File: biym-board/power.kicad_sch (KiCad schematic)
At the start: 6 parts, among them J1 JST_SH_BM02_VERTICAL, Q1 MOSFET-N-CH-EN, Q2 MOSFET-P-CH-EN

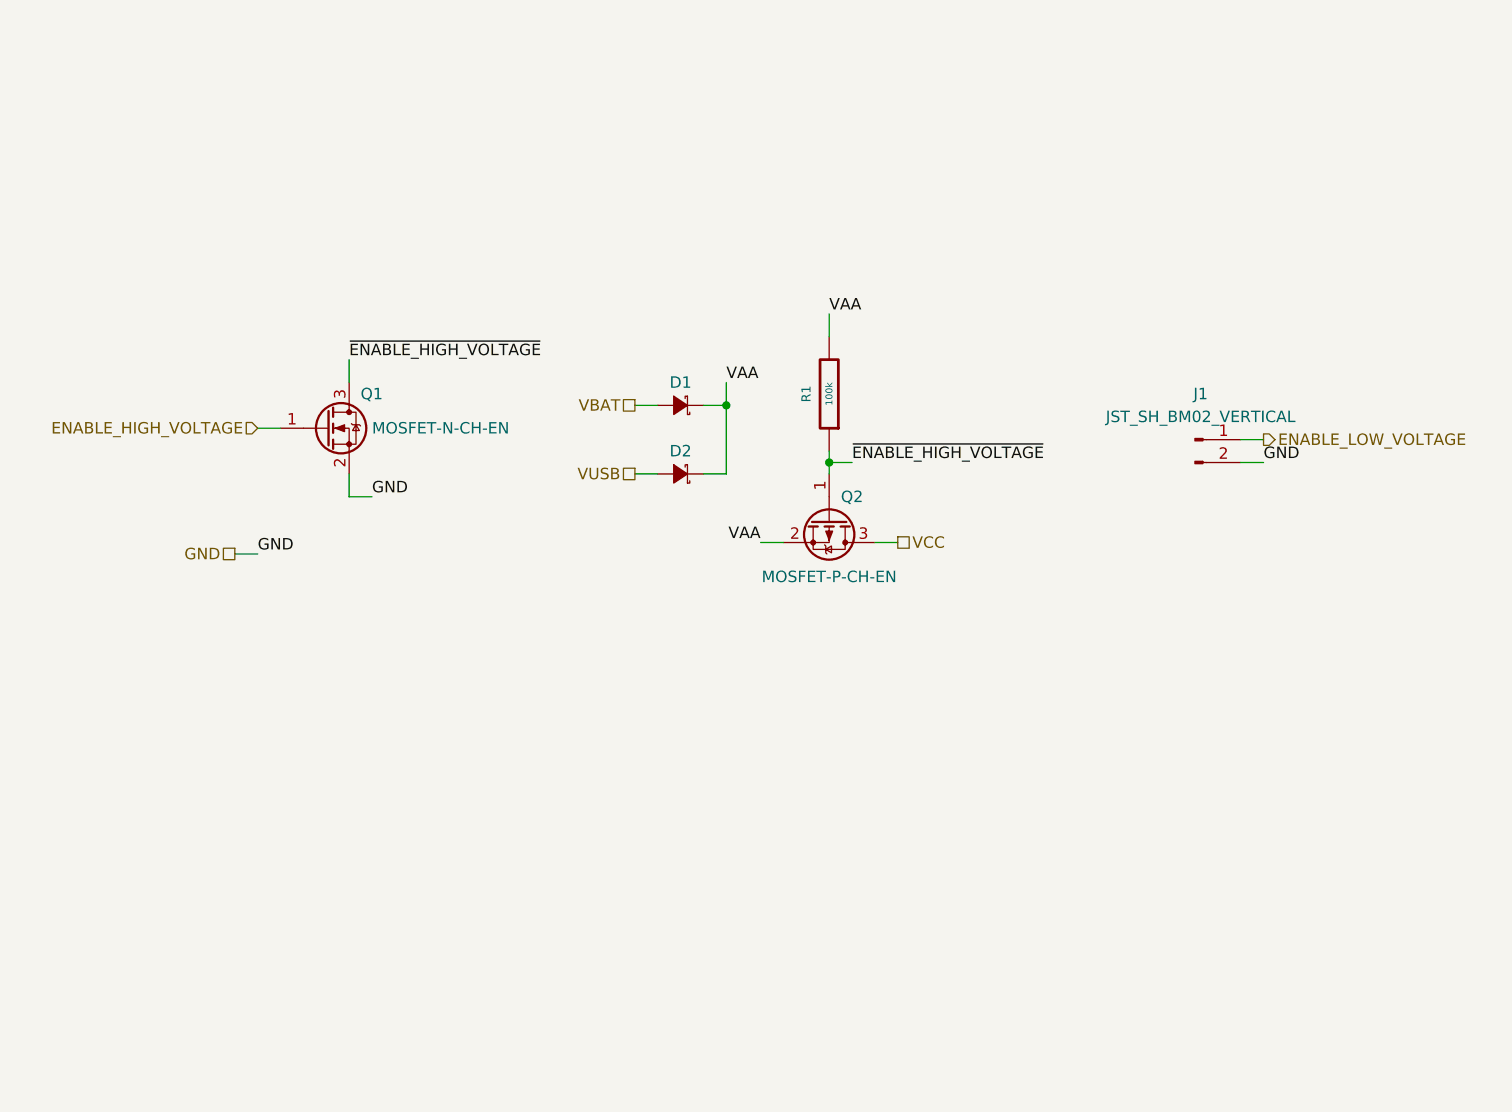
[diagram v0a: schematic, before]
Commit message: Change diodes
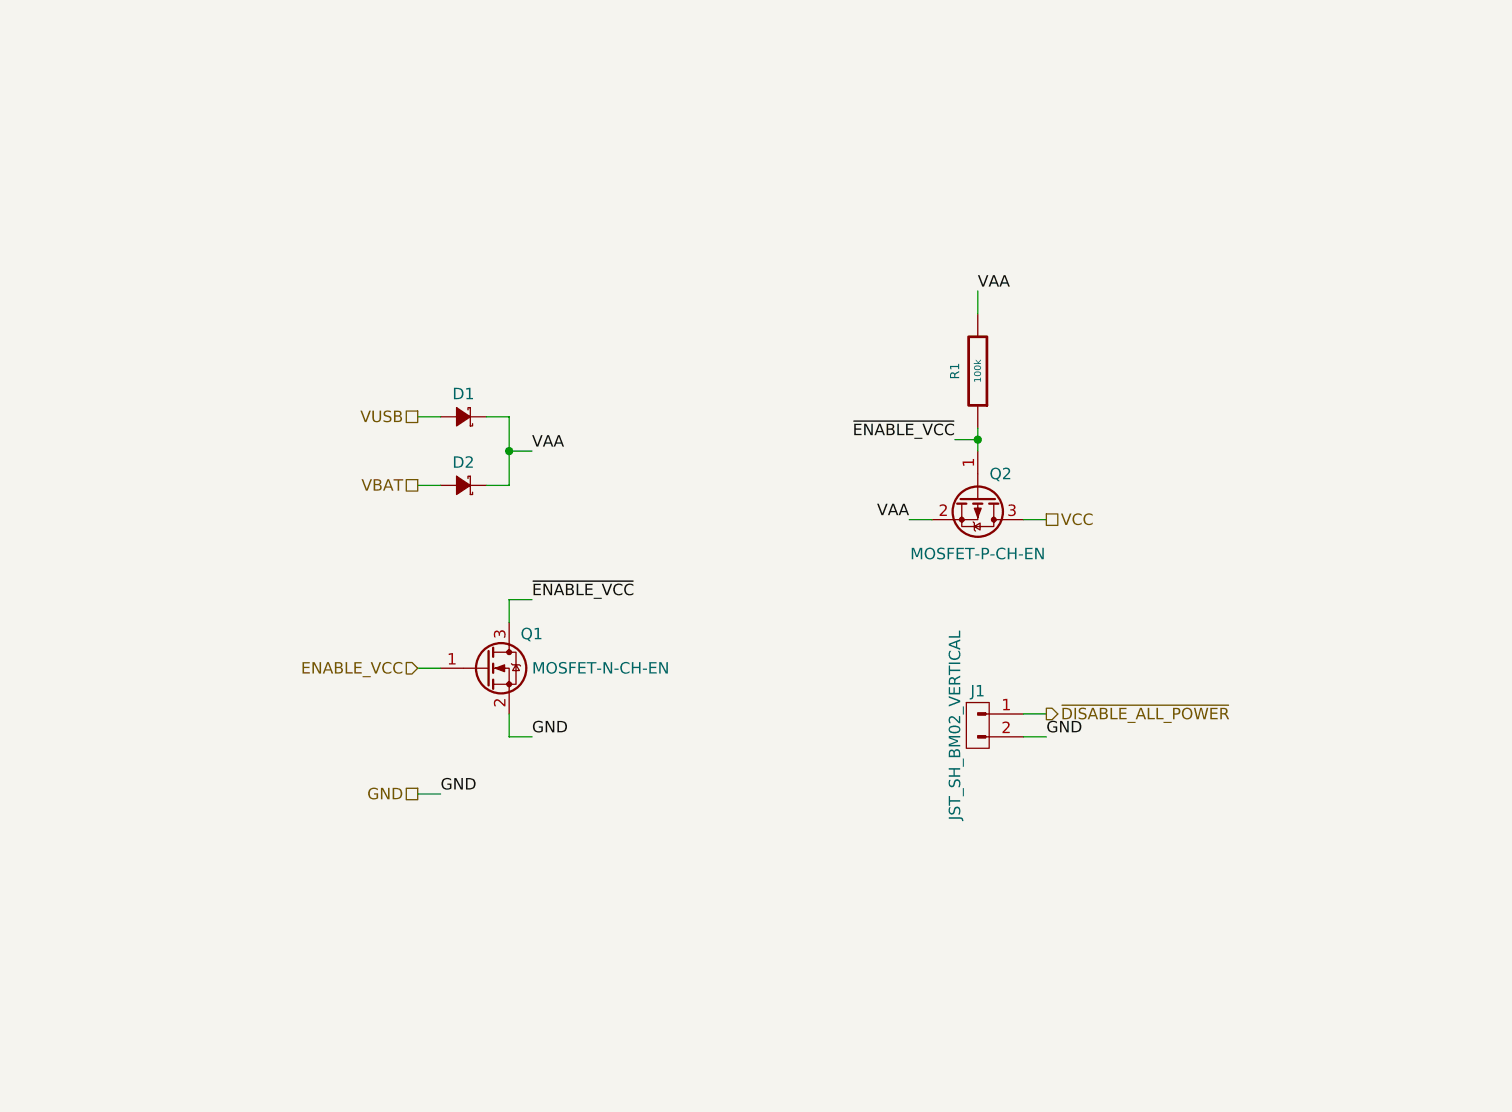
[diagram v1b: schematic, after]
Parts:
- removed D1, D2: DIODE_SCHOTTKY_15V_1A, footprints:DO-214BA, symbol Janelia:DIODE_SCHOTTKY_15V_1A
- added D1, D2: DIODE_SCHOTTKY_40V_2A_0603, Janelia:SM0603_DSN2, symbol Janelia:DIODE_SCHOTTKY_40V_2A_0603
- R1: footprint footprints:SM0402 -> Janelia:SM0402
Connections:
- net VAA: now also D1.1 (K), D2.1 (K)
- net VBAT: now also D2.2 (A)
- net VUSB: now also D1.2 (A)
- net ENABLE_HIGH_VOLTAGE renamed ENABLE_VCC
- net ENABLE_LOW_VOLTAGE renamed ~{DISABLE_ALL_POWER}
- net ~{ENABLE_HIGH_VOLTAGE} renamed ~{ENABLE_VCC}
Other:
- title: (none) -> biym-board-power
- moved on the sheet: Q1, Q2, R1

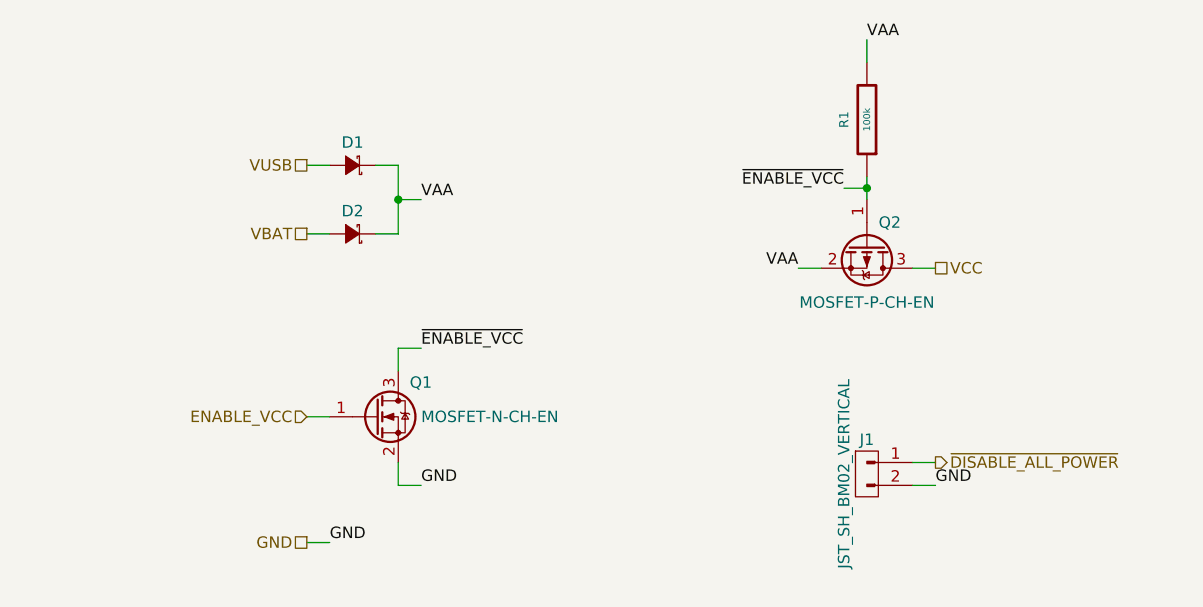
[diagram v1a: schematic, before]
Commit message: Switch feather contacts to pogo pins
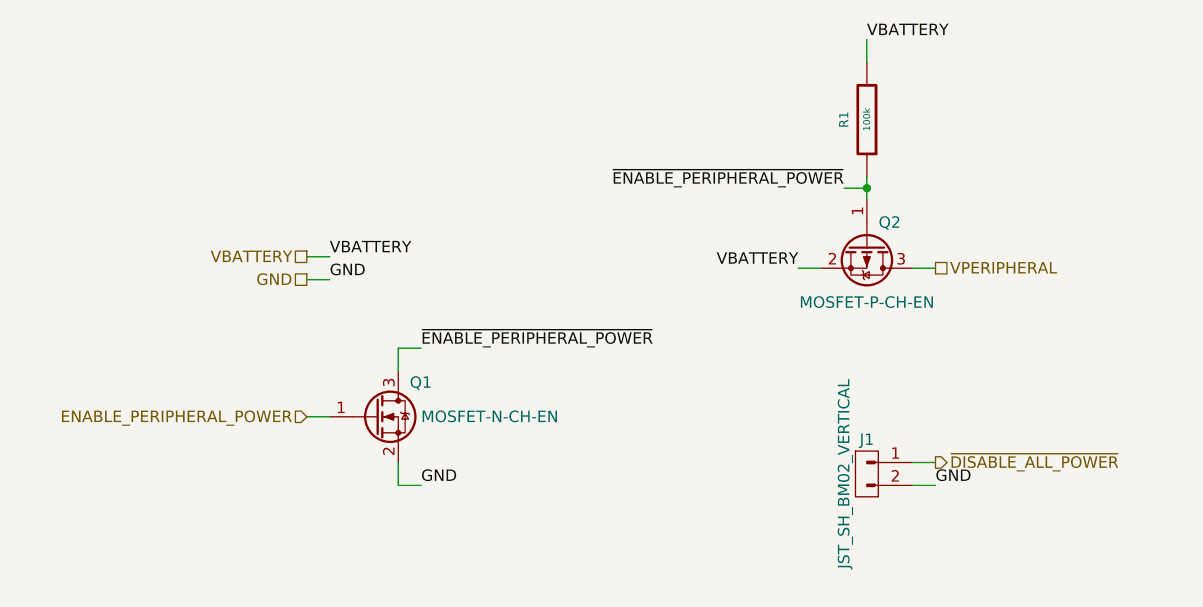
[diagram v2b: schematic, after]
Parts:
- removed D1, D2: DIODE_SCHOTTKY_40V_2A_0603, Janelia:SM0603_DSN2, symbol Janelia:DIODE_SCHOTTKY_40V_2A_0603
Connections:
- net ENABLE_VCC renamed ENABLE_PERIPHERAL_POWER
- net VAA renamed VBATTERY
- net VCC renamed VPERIPHERAL
- net ~{ENABLE_VCC} renamed ~{ENABLE_PERIPHERAL_POWER}
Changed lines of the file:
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@@
     (date "2022-11-10")
-  )
-  (junction (at 111.76 88.9) (diameter 0) (color 0 0 0 0)
   )
   (junction (at 163.83 87.63) (diameter 0) (color 0 0 0 0)
   )
   (wire (pts (xy 111.76 118.11) (xy 111.76 120.65))
-    (stroke (width 0) (type default) (color 0 0 0 0))
-  )
-  (wire (pts (xy 109.22 92.71) (xy 111.76 92.71))
     (stroke (width 0) (type default) (color 0 0 0 0))
   )
@@
     (stroke (width 0) (type default) (color 0 0 0 0))
   )
-  (wire (pts (xy 109.22 85.09) (xy 111.76 85.09))
+  (wire (pts (xy 101.6 95.25) (xy 104.14 95.25))
     (stroke (width 0) (type default) (color 0 0 0 0))
   )
@@
     (stroke (width 0) (type default) (color 0 0 0 0))
   )
-  (wire (pts (xy 111.76 88.9) (xy 114.3 88.9))
-    (stroke (width 0) (type default) (color 0 0 0 0))
-  )
-  (wire (pts (xy 111.76 88.9) (xy 111.76 92.71))
-    (stroke (width 0) (type default) (color 0 0 0 0))
-  )
-  (wire (pts (xy 101.6 127) (xy 104.14 127))
+  (wire (pts (xy 101.6 97.79) (xy 104.14 97.79))
     (stroke (width 0) (type default) (color 0 0 0 0))
   )
@@
     (stroke (width 0) (type default) (color 0 0 0 0))
   )
-  (wire (pts (xy 111.76 85.09) (xy 111.76 88.9))
-    (stroke (width 0) (type default) (color 0 0 0 0))
-  )
-  (wire (pts (xy 104.14 85.09) (xy 101.6 85.09))
-    (stroke (width 0) (type default) (color 0 0 0 0))
-  )
-  (wire (pts (xy 104.14 92.71) (xy 101.6 92.71))
-    (stroke (width 0) (type default) (color 0 0 0 0))
-  )
   (wire (pts (xy 168.91 96.52) (xy 171.45 96.52))
     (stroke (width 0) (type default) (color 0 0 0 0))
@@
     (stroke (width 0) (type default) (color 0 0 0 0))
   )
-  (label "~{ENABLE_VCC}" (at 161.29 87.63 180)
+  (label "~{ENABLE_PERIPHERAL_POWER}" (at 161.29 87.63 180)
     (effects (font (size 1.27 1.27)) (justify right bottom))
   )
@@
     (effects (font (size 1.27 1.27)) (justify left bottom))
   )
-  (label "VAA" (at 114.3 88.9 0)
+  (label "VBATTERY" (at 163.83 71.12 0)
     (effects (font (size 1.27 1.27)) (justify left bottom))
   )
-  (label "VAA" (at 163.83 71.12 0)
-    (effects (font (size 1.27 1.27)) (justify left bottom))
-  )
-  (label "VAA" (at 156.21 96.52 180)
+  (label "VBATTERY" (at 156.21 96.52 180)
     (effects (font (size 1.27 1.27)) (justify right bottom))
   )
@@
     (effects (font (size 1.27 1.27)) (justify left bottom))
   )
-  (label "GND" (at 104.14 127 0)
+  (label "VBATTERY" (at 104.14 95.25 0)
     (effects (font (size 1.27 1.27)) (justify left bottom))
   )
-  (label "~{ENABLE_VCC}" (at 114.3 105.41 0)
+  (label "GND" (at 104.14 97.79 0)
     (effects (font (size 1.27 1.27)) (justify left bottom))
   )
-  (hierarchical_label "VCC" (shape passive) (at 171.45 96.52 0)
+  (label "~{ENABLE_PERIPHERAL_POWER}" (at 114.3 105.41 0)
+    (effects (font (size 1.27 1.27)) (justify left bottom))
+  )
+  (hierarchical_label "VPERIPHERAL" (shape passive) (at 171.45 96.52 0)
     (effects (font (size 1.27 1.27)) (justify left))
   )
-  (hierarchical_label "GND" (shape passive) (at 101.6 127 180)
+  (hierarchical_label "GND" (shape passive) (at 101.6 97.79 180)
     (effects (font (size 1.27 1.27)) (justify right))
   )
-  (hierarchical_label "VBAT" (shape passive) (at 101.6 92.71 180)
+  (hierarchical_label "VBATTERY" (shape passive) (at 101.6 95.25 180)
     (effects (font (size 1.27 1.27)) (justify right))
   )
-  (hierarchical_label "VUSB" (shape passive) (at 101.6 85.09 180)
-    (effects (font (size 1.27 1.27)) (justify right))
-  )
-  (hierarchical_label "ENABLE_VCC" (shape input) (at 101.6 113.03 180)
+  (hierarchical_label "ENABLE_PERIPHERAL_POWER" (shape input) (at 101.6 113.03 180)
     (effects (font (size 1.27 1.27)) (justify right))
   )
@@
     (pin "3")
   )
-  (symbol (lib_id "Janelia:DIODE_SCHOTTKY_40V_2A_0603") (at 106.68 92.71 180) (unit 1)
-    (in_bom yes) (on_board yes)
-    (property "Reference" "D2" (id 0) (at 106.68 90.17 0))
-    (property "Value" "DIODE_SCHOTTKY_40V_2A_0603" (id 1) (at 121.92 107.95 0)
-      (effects (font (size 1.27 1.27)) (justify left) hide)
-    )
-    (property "Footprint" "Janelia:SM0603_DSN2" (id 2) (at 106.68 105.41 0)
-      (effects (font (size 1.524 1.524)) hide)
-    )
-    (property "Datasheet" "" (id 3) (at 107.95 94.742 0)
-      (effects (font (size 1.524 1.524)) hide)
-    )
-    (property "Vendor" "Digi-Key" (id 4) (at 105.41 97.282 0)
-      (effects (font (size 1.524 1.524)) hide)
-    )
-    (property "Vendor Part Number" "NSR20F40NXT5GOSCT-ND" (id 5) (at 102.87 99.822 0)
-      (effects (font (size 1.524 1.524)) hide)
-    )
-    (property "Description" "DIODE SCHOTTKY 40V 2A 2DSN" (id 6) (at 100.33 102.362 0)
-      (effects (font (size 1.524 1.524)) hide)
-    )
-    (property "Manufacturer" "onsemi" (id 7) (at 106.68 110.49 0)
-      (effects (font (size 1.27 1.27)) hide)
-    )
-    (property "Manufacturer Part Number" "NSR20F40NXT5G" (id 8) (at 106.68 113.03 0)
-      (effects (font (size 1.27 1.27)) hide)
-    )
-    (pin "1")
-    (pin "2")
-  )
   (symbol (lib_id "Janelia:MOSFET-N-CH-EN-DMG2302UKQ-7") (at 109.22 113.03 0) (unit 1)
     (in_bom yes) (on_board yes)
@@
     (pin "3")
   )
-  (symbol (lib_id "Janelia:DIODE_SCHOTTKY_40V_2A_0603") (at 106.68 85.09 180) (unit 1)
-    (in_bom yes) (on_board yes)
-    (property "Reference" "D1" (id 0) (at 106.68 82.55 0))
-    (property "Value" "DIODE_SCHOTTKY_40V_2A_0603" (id 1) (at 121.92 100.33 0)
-      (effects (font (size 1.27 1.27)) (justify left) hide)
-    )
-    (property "Footprint" "Janelia:SM0603_DSN2" (id 2) (at 106.68 97.79 0)
-      (effects (font (size 1.524 1.524)) hide)
-    )
-    (property "Datasheet" "" (id 3) (at 107.95 87.122 0)
-      (effects (font (size 1.524 1.524)) hide)
-    )
-    (property "Vendor" "Digi-Key" (id 4) (at 105.41 89.662 0)
-      (effects (font (size 1.524 1.524)) hide)
-    )
-    (property "Vendor Part Number" "NSR20F40NXT5GOSCT-ND" (id 5) (at 102.87 92.202 0)
-      (effects (font (size 1.524 1.524)) hide)
-    )
-    (property "Description" "DIODE SCHOTTKY 40V 2A 2DSN" (id 6) (at 100.33 94.742 0)
-      (effects (font (size 1.524 1.524)) hide)
-    )
-    (property "Manufacturer" "onsemi" (id 7) (at 106.68 102.87 0)
-      (effects (font (size 1.27 1.27)) hide)
-    )
-    (property "Manufacturer Part Number" "NSR20F40NXT5G" (id 8) (at 106.68 105.41 0)
-      (effects (font (size 1.27 1.27)) hide)
-    )
-    (pin "1")
-    (pin "2")
-  )
   (symbol (lib_id "Janelia:JST_SH_BM02_VERTICAL") (at 163.83 118.11 0) (unit 1)

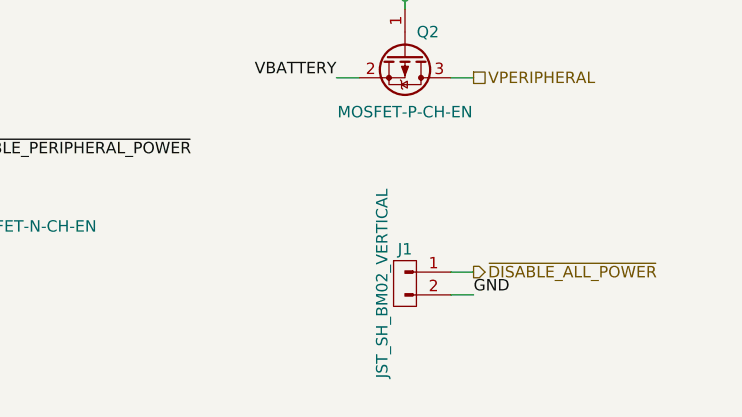
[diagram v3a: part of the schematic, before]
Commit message: Rename reference files
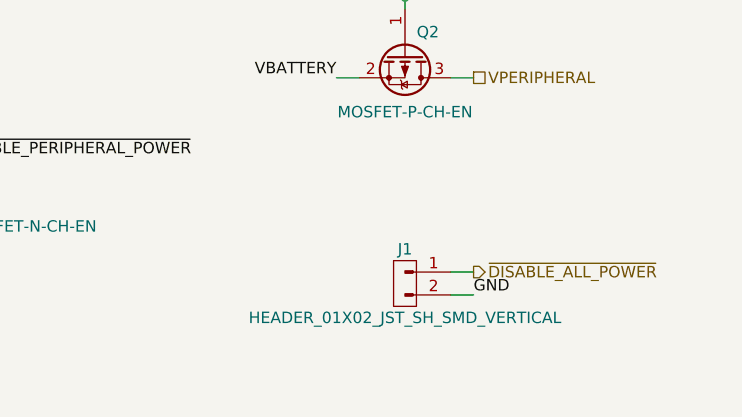
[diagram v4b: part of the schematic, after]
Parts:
- removed J1: JST_SH_BM02_VERTICAL, Janelia:JST_SH_BM02B-SRSS-TB_1x02-1MP_P1.00mm_Vertical, symbol Janelia:JST_SH_BM02_VERTICAL
- added J1: HEADER_01X02_JST_SH_SMD_VERTICAL, Janelia:JST_SH_BM02B-SRSS-TB_1x02-1MP_P1.00mm_Vertical, symbol Janelia:HEADER_01X02_JST_SH_SMD_VERTICAL
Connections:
- net GND: now also J1.2 (Pin_2)
- net ~{DISABLE_ALL_POWER}: now also J1.1 (Pin_1)
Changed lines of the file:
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@@
     (pin "3")
   )
-  (symbol (lib_id "Janelia:JST_SH_BM02_VERTICAL") (at 163.83 118.11 0) (unit 1)
+  (symbol (lib_id "Janelia:HEADER_01X02_JST_SH_SMD_VERTICAL") (at 163.83 118.11 0) (unit 1)
     (in_bom yes) (on_board yes)
     (property "Reference" "J1" (id 0) (at 163.83 115.57 0))
-    (property "Value" "JST_SH_BM02_VERTICAL" (id 1) (at 161.29 119.38 90))
+    (property "Value" "HEADER_01X02_JST_SH_SMD_VERTICAL" (id 1) (at 163.83 123.19 0))
     (property "Footprint" "Janelia:JST_SH_BM02B-SRSS-TB_1x02-1MP_P1.00mm_Vertical" (id 2) (at 163.83 105.41 0)
       (effects (font (size 1.27 1.27)) hide)
